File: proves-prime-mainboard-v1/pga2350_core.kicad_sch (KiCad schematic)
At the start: 22 parts, among them IC2 AZ1117CH-3.3TRG1, SW1 KMR2, SW2 KMR2, SW3 SW_SPDT

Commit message: Started the Schematic Layout
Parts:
- removed C12: 10uF, Capacitor_SMD:C_0603_1608Metric, symbol Adafruit ItsyBitsy RP2040-eagle-import:CAP_CERAMIC_0603MP
- removed C13: 22uF, Capacitor_SMD:C_0603_1608Metric, symbol Adafruit ItsyBitsy RP2040-eagle-import:CAP_CERAMIC_0603MP
- removed D8: NSR0320, Diode_SMD:D_SOD-323F, symbol Diode:1SS355VM
- removed IC2: AZ1117CH-3.3TRG1, Package_TO_SOT_SMD:SOT-223, symbol AZ1117CH-3.3TRG1:AZ1117CH-3.3TRG1
- removed R36: 1k, Resistor_SMD:R_0603_1608Metric, symbol mainboard:RESISTOR0603
- removed SW3: SW_SPDT, symbol Switch:SW_SPDT
- added R1: 10k, Resistor_SMD:R_0603_1608Metric, symbol mainboard:RESISTOR0603
- added SW4: SW_SPDT, symbol Switch:SW_SPDT
- R4, R5: value 1k -> 10k
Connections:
- net FC_RESET is gone; now on net ~{RESET}: SW2.A (P), SW2.A' (P1), TP8.1
- net +3V3: now also A1.55 (3V3), R1.1
- net USBBOOT: now also A1.48 (BOOTSEL)
- net ~{RESET}: now reaches A1.54 (RUN)
- net ~{RESET}: now also R1.2
- net at A1.56 (3V3_EN): now also SW4.2 (B)
- net NEOPIX: now reaches LED1.4 (DI)
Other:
- note added: "Check if USBBOOT Needs Pull Up"
- note added: "Status LEDs"
- note added: "Throw to Enable Backup USB Power"
- note removed: "3v3 Linear Regulator"
- note removed: "For USB Power"
- moved on the sheet: A1, D1, D2, D3, D9, JP1, R38, R4, R5, R6, SW1, SW2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

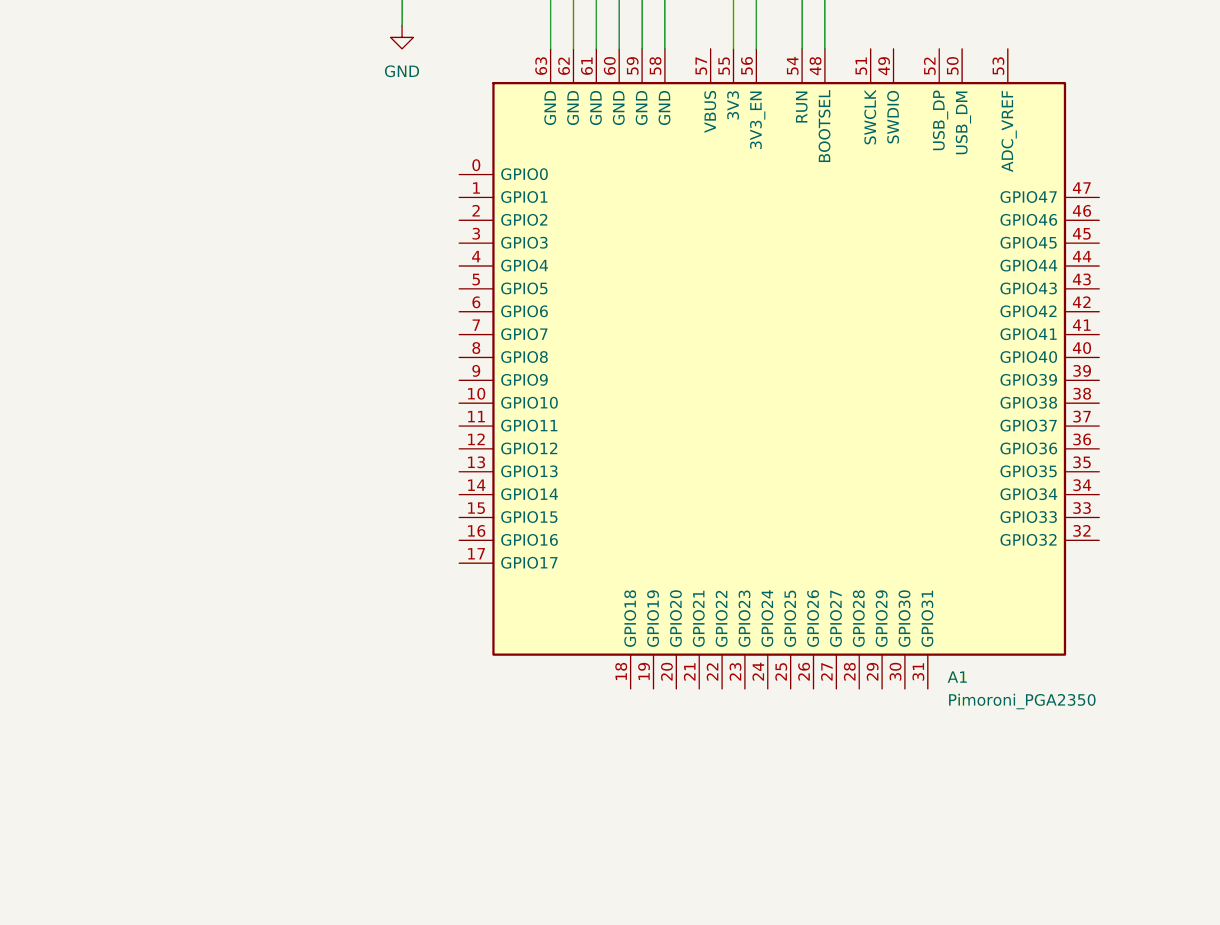
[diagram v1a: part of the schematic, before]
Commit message: Updated PGA2350 Symbol
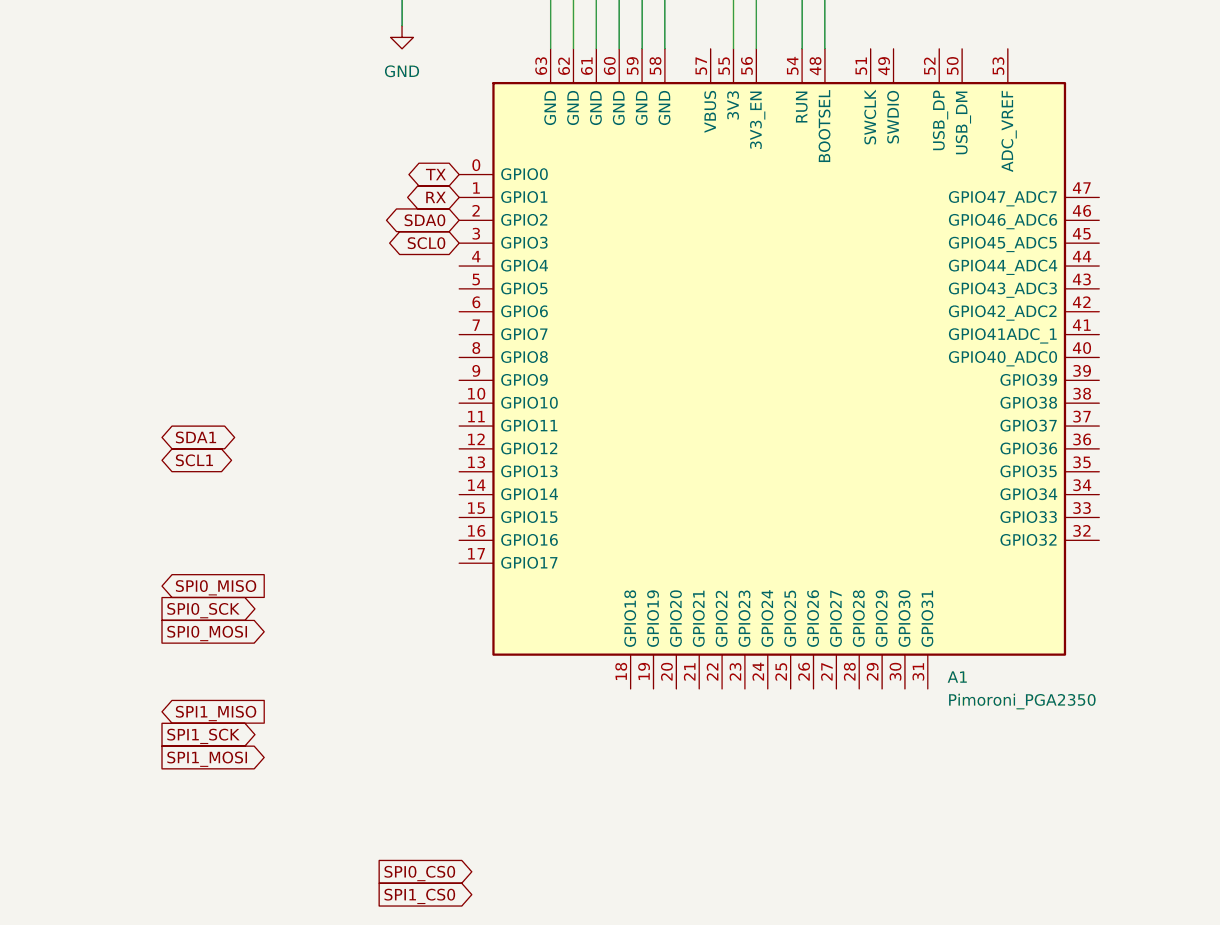
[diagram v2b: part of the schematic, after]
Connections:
- net RX: now also A1.1 (GPIO1)
- net TX: now also A1.0 (GPIO0)
- net SDA0: now reaches A1.2 (GPIO2)
- net SCL0: now reaches A1.3 (GPIO3)

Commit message: DSAFASDFASDF
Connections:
- net RX: no longer A1.1 (GPIO1)
- net SPI0_CS0: now also A1.5 (GPIO5)
- net SPI0_MISO: now also A1.4 (GPIO4)
- net SPI0_MOSI: now also A1.7 (GPIO7)
- net SPI0_SCK: now also A1.6 (GPIO6)
- net SPI1_CS0: now also A1.29 (GPIO29)
- net SPI1_MISO: now also A1.28 (GPIO28)
- net SPI1_MOSI: now also A1.31 (GPIO31)
- net SPI1_SCK: now also A1.30 (GPIO30)
- net TX: no longer A1.0 (GPIO0)
- net I2C0_SDA: now reaches A1.32 (GPIO32)
- net I2C0_SCL: now reaches A1.33 (GPIO33)
- net UART1_TX: now reaches A1.36 (GPIO36)
- net UART1_RX: now reaches A1.37 (GPIO37)
- net UART1_CTS: now reaches A1.38 (GPIO38)
- net UART1_RTS: now reaches A1.39 (GPIO39)
- net SCL0 renamed I2C1_SCL
- net SDA0 renamed I2C1_SDA
- new net UART0_RX: A1.1 (GPIO1)
- new net UART0_TX: A1.0 (GPIO0)

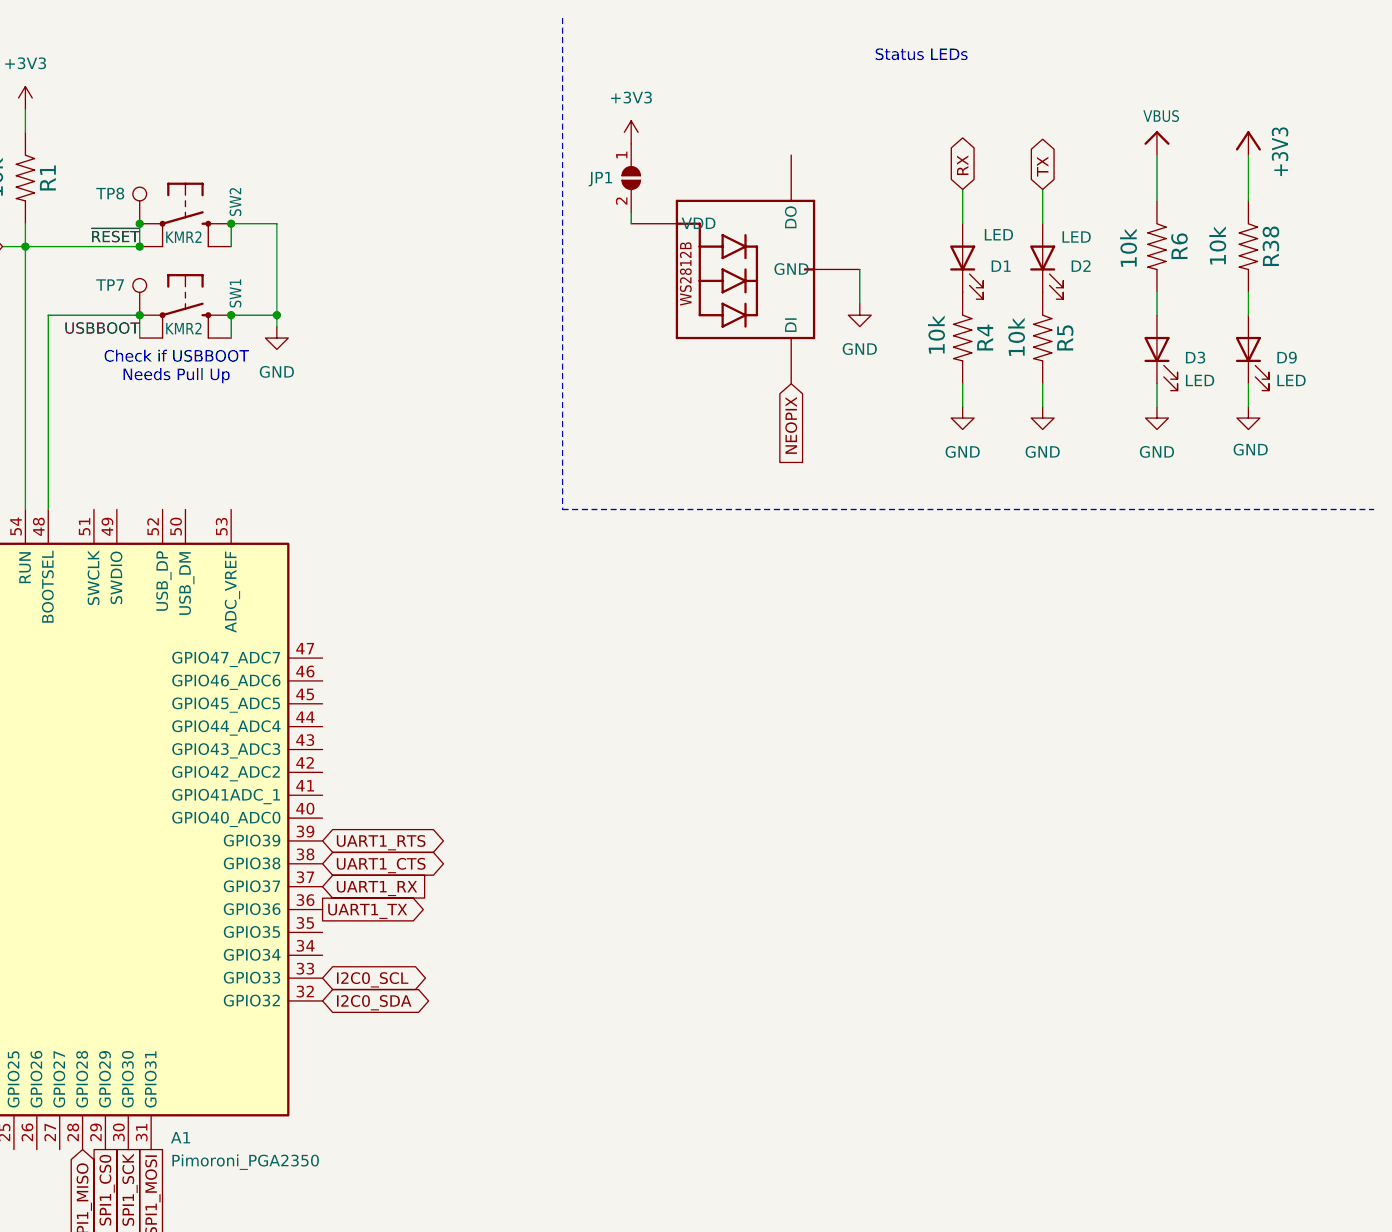
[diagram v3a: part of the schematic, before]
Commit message: Added USB-C Connector
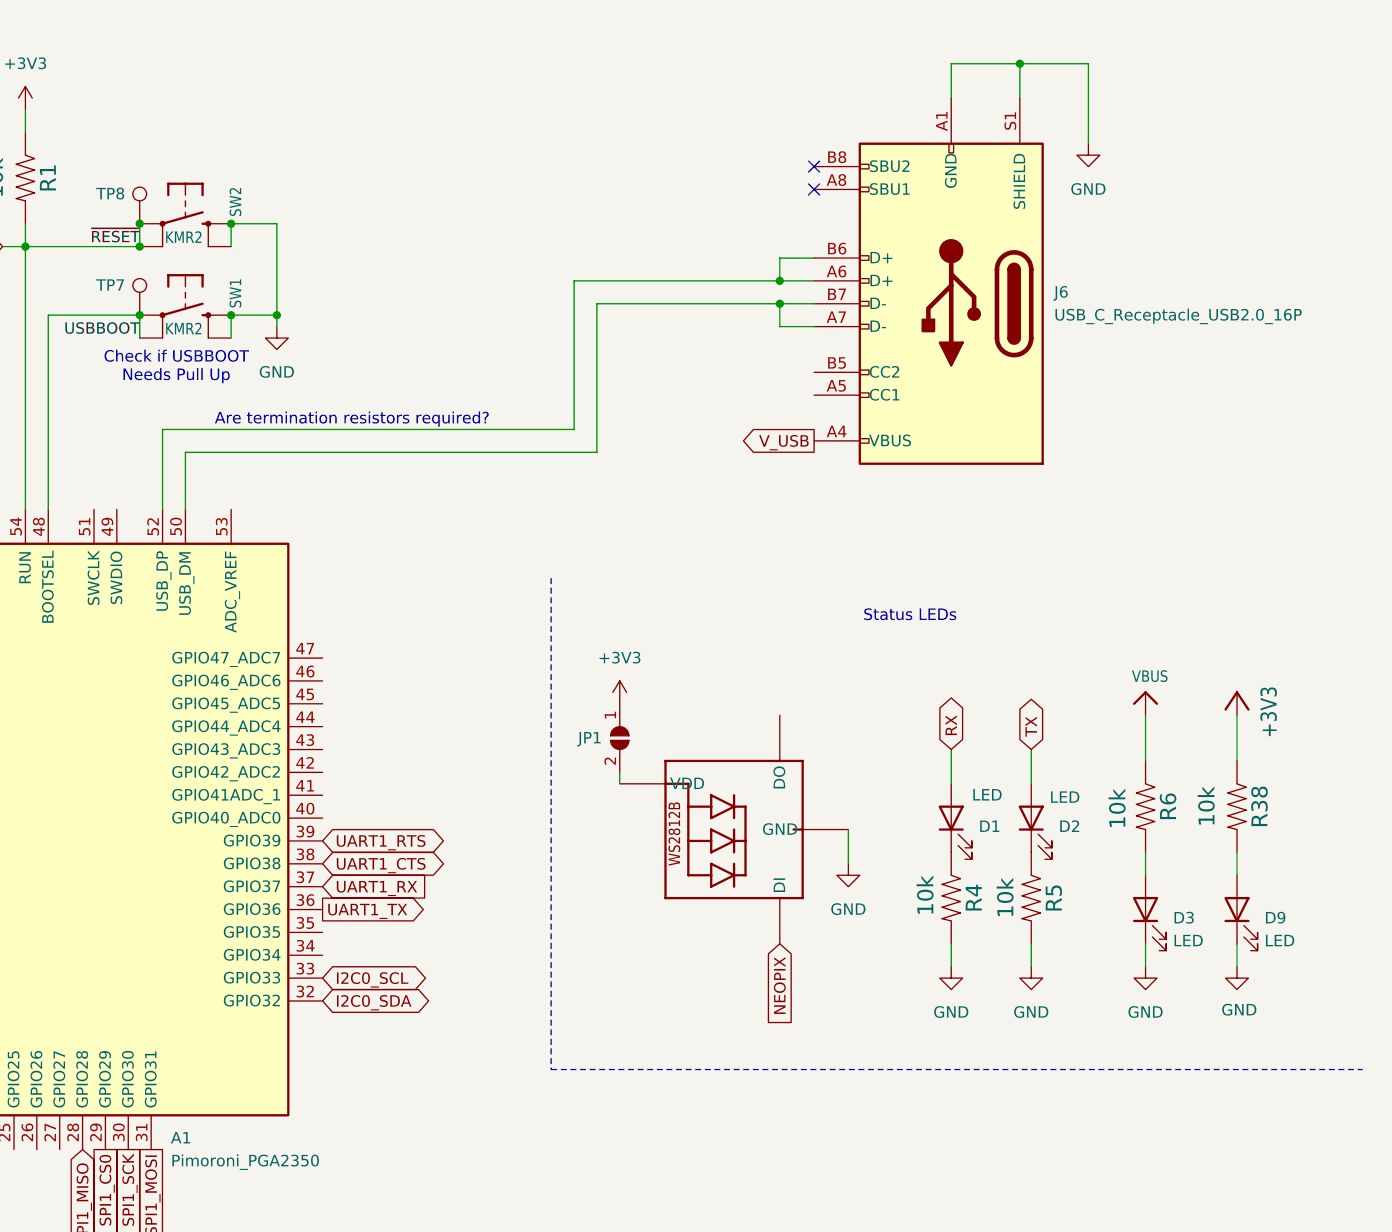
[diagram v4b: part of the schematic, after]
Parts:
- added J6: USB_C_Receptacle_USB2.0_16P, Connector_USB:USB_C_Receptacle_HRO_TYPE-C-31-M-12, symbol Connector:USB_C_Receptacle_USB2.0_16P
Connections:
- net GND: now also J6.A1 (GND), J6.A12 (GND), J6.B1 (GND), J6.B12 (GND), J6.S1 (SHIELD)
- net at A1.50 (USB_DM): now also J6.A7 (D-), J6.B7 (D-)
- net at A1.52 (USB_DP): now also J6.A6 (D+), J6.B6 (D+)
- new net V_USB: J6.A4 (VBUS), J6.A9 (VBUS), J6.B4 (VBUS), J6.B9 (VBUS)
- no-connect marks 0 -> 2
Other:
- note added: "Are termination resistors required?"
- moved on the sheet: D1, D2, D3, D9, JP1, R38, R4, R5, R6

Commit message: More Wiring!
Connected Additional Peripheral
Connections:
- net RX is gone; now on net UART0_RX: D1.2 (A)
- net TX is gone; now on net UART0_TX: D2.2 (A)
- net GND: now also SW4.3 (C)
- net NEOPIX: now also A1.47 (GPIO47_ADC7)
- net V_USB: now also A1.57 (VBUS), SW4.1 (A)
- net RF1_IO4: now reaches A1.10 (GPIO10)
- net RF1_IO0: now reaches A1.11 (GPIO11)
- net RF2_RST: now reaches A1.12 (GPIO12)
- net RF2_IO4: now reaches A1.13 (GPIO13)
- net RF2_IO0: now reaches A1.14 (GPIO14)
- net ENABLE_3V3: now reaches A1.18 (GPIO18)
- net ENABLE_5V: now reaches A1.19 (GPIO19)
- net ~{CHARGE}: now reaches A1.20 (GPIO20)
- net WDT_WDI: now reaches A1.24 (GPIO24)
- net SWDIO: now reaches A1.49 (SWDIO)
- net SWCLK: now reaches A1.51 (SWCLK)
- net RTC_INT: now reaches A1.8 (GPIO8)
- net RF1_RST: now reaches A1.9 (GPIO9)
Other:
- note added: "CHECK E9 ERATA"

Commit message: Added Mux
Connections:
- net RF1_IO0: now also A1.12 (GPIO12); no longer A1.11 (GPIO11)
- net RF1_IO4: now also A1.11 (GPIO11); no longer A1.10 (GPIO10)
- net RF1_RST: now also A1.10 (GPIO10); no longer A1.9 (GPIO9)
- net RF2_IO0: now also A1.15 (GPIO15); no longer A1.14 (GPIO14)
- net RF2_IO4: now also A1.14 (GPIO14); no longer A1.13 (GPIO13)
- net RF2_RST: now also A1.13 (GPIO13); no longer A1.12 (GPIO12)
- net RTC_INT: now also A1.9 (GPIO9); no longer A1.8 (GPIO8)
- new net ~{MUX_RESET}: A1.8 (GPIO8)

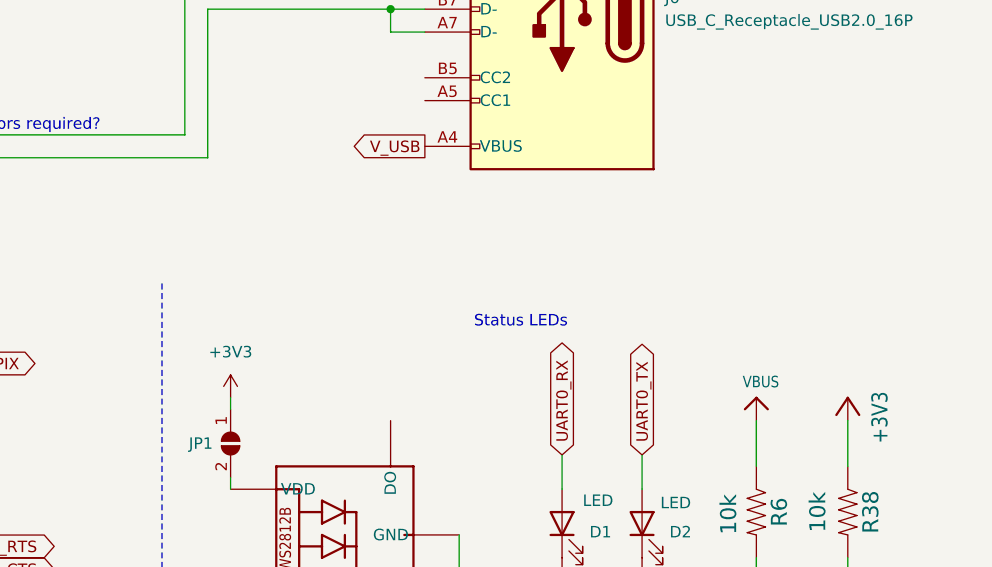
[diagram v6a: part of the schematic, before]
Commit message: Added Burnwire Candidates
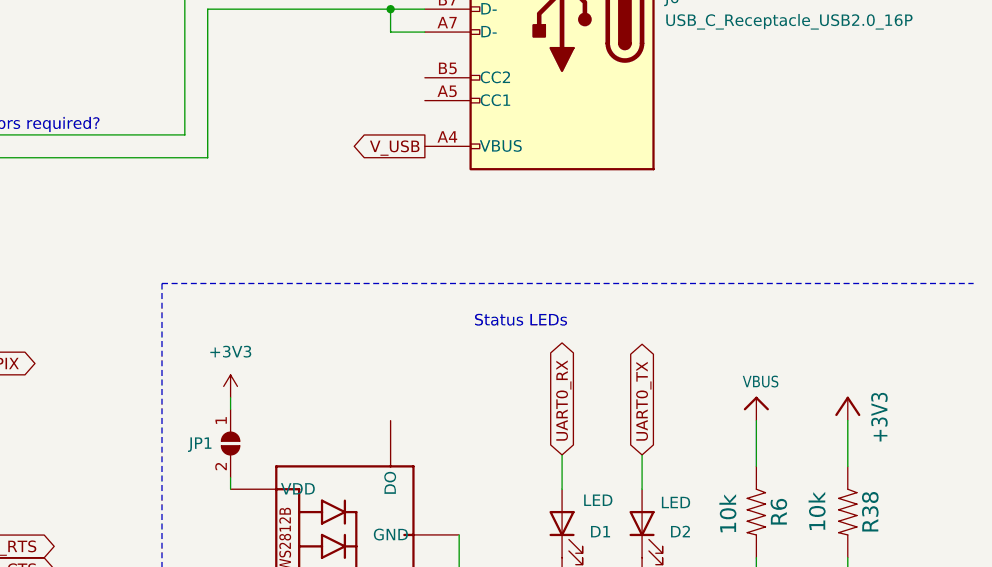
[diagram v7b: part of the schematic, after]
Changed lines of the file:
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@@
+		)
+	)
+	(polyline
+		(pts
+			(xy 194.31 73.66) (xy 284.48 73.66)
+		)
+		(stroke
+			(width 0)
+			(type dash)
 		)
 	)
